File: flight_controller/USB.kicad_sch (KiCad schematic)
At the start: 11 parts, among them J9 TYPE-C16PIN2MD(073) (USB TYPE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, U5 SN74LVC1G07DBVR_C19829659

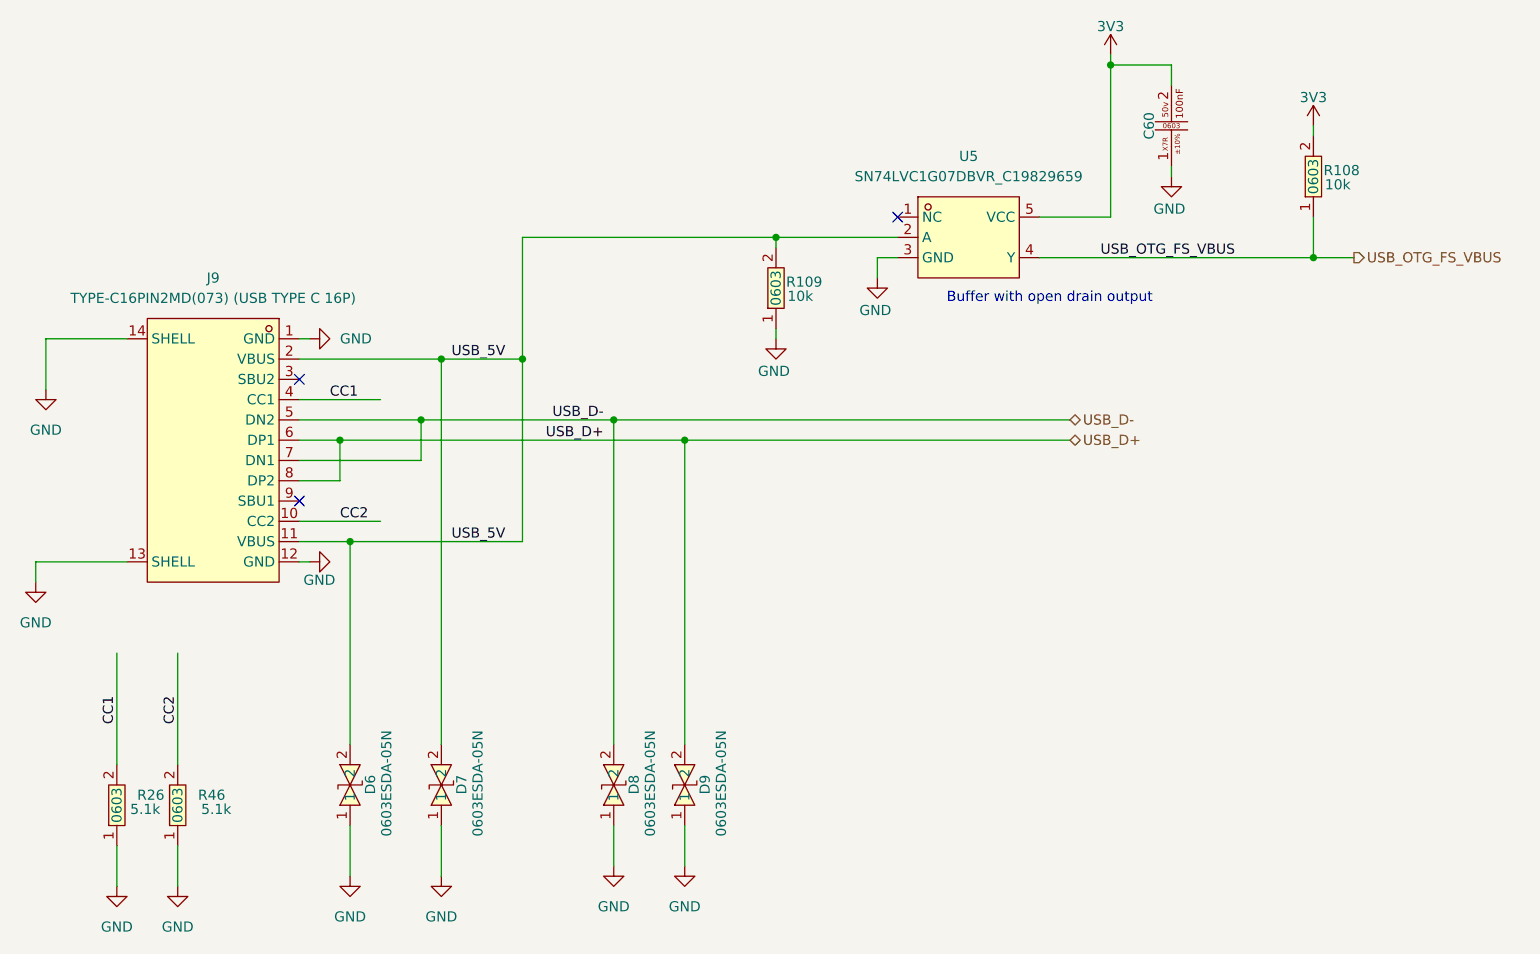
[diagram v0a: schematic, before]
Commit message: Started the placement process
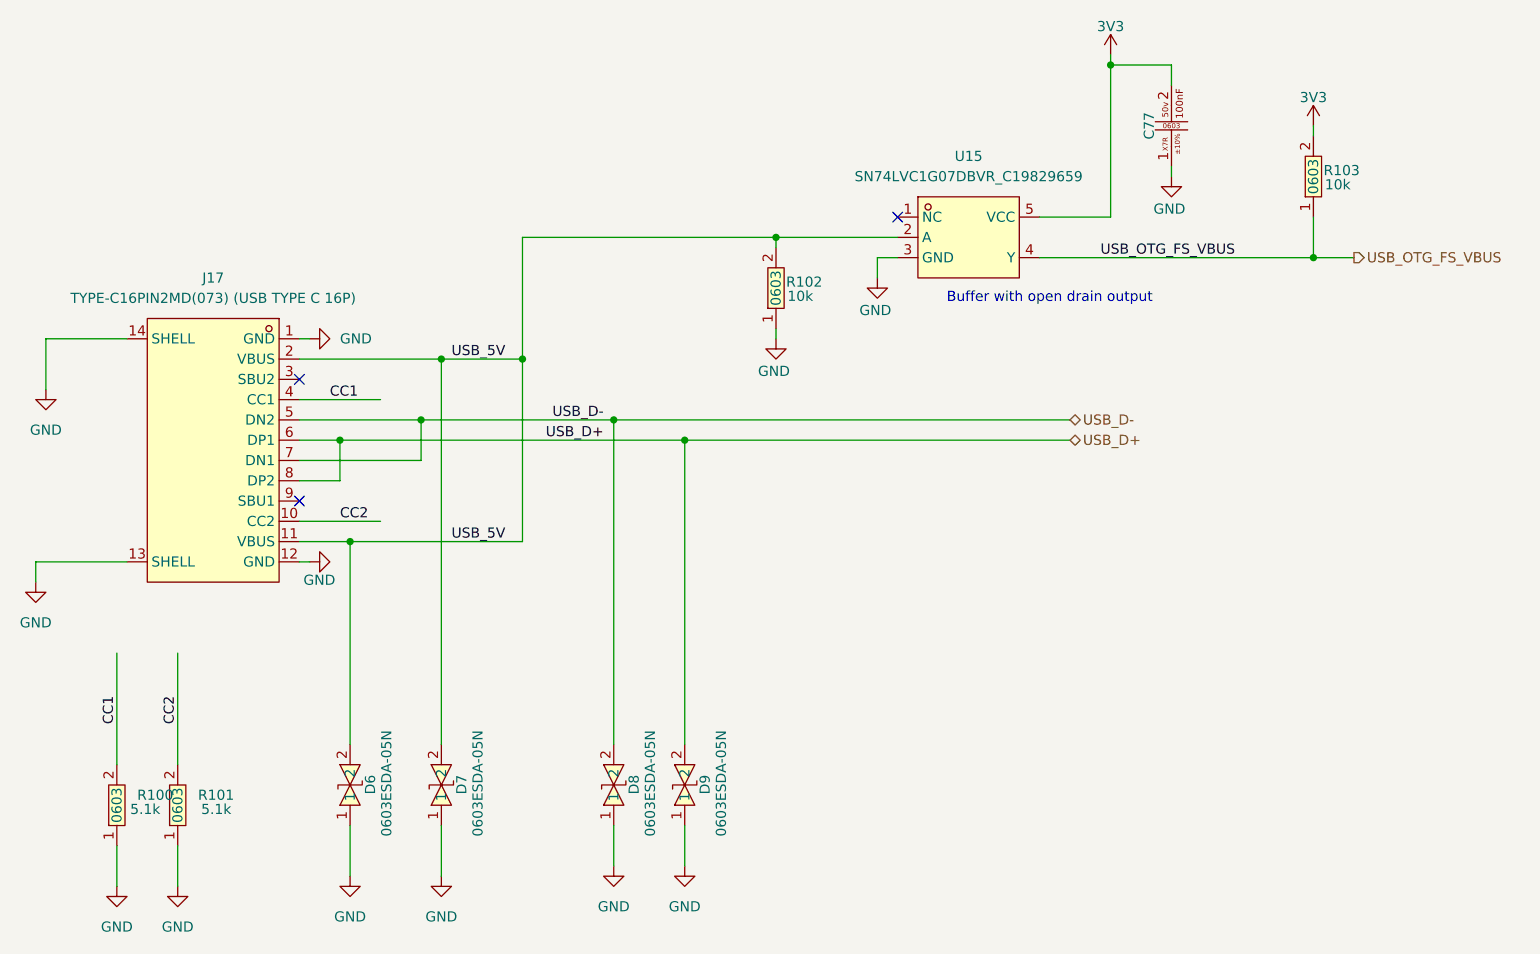
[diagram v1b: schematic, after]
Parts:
- renumbered C60 to C77, J9 to J17, R26 to R100, R46 to R101, R109 to R102, R108 to R103, U5 to U15
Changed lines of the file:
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@@
 		(on_board yes)
 		(dnp no)
-		(property "Reference" "#PWR0183"
+		(property "Reference" "#PWR0213"
 			(at 218.44 25.4 0)
 			(effects
@@
 			(project "FP_BOARD"
 				(path "/17737359-1a8e-4237-8899-d9604030bc1d/9d897fa1-9f20-45cb-8d2c-42b78b3f3ef1"
-					(reference "#PWR0183")
+					(reference "#PWR0213")
 					(unit 1)
 				)
@@
 		(dnp no)
 		(fields_autoplaced yes)
-		(property "Reference" "#PWR0415"
+		(property "Reference" "#PWR0208"
 			(at 134.62 130.81 0)
 			(effects
@@
 			(project "FP_BOARD"
 				(path "/17737359-1a8e-4237-8899-d9604030bc1d/9d897fa1-9f20-45cb-8d2c-42b78b3f3ef1"
-					(reference "#PWR0415")
+					(reference "#PWR0208")
 					(unit 1)
 				)
@@
 		(on_board yes)
 		(dnp no)
-		(property "Reference" "#PWR0412"
+		(property "Reference" "#PWR0206"
 			(at 124.46 85.09 0)
 			(effects
@@
 			(project "FP_BOARD"
 				(path "/17737359-1a8e-4237-8899-d9604030bc1d/9d897fa1-9f20-45cb-8d2c-42b78b3f3ef1"
-					(reference "#PWR0412")
+					(reference "#PWR0206")
 					(unit 1)
 				)
@@
 		(on_board yes)
 		(dnp no)
-		(property "Reference" "#PWR0195"
+		(property "Reference" "#PWR0211"
 			(at 176.53 63.5 0)
 			(effects
@@
 			(project "FP_BOARD"
 				(path "/17737359-1a8e-4237-8899-d9604030bc1d/9d897fa1-9f20-45cb-8d2c-42b78b3f3ef1"
-					(reference "#PWR0195")
+					(reference "#PWR0211")
 					(unit 1)
 				)
@@
 		(dnp no)
 		(fields_autoplaced yes)
-		(property "Reference" "#PWR0417"
+		(property "Reference" "#PWR0210"
 			(at 165.1 129.54 0)
 			(effects
@@
 			(project "FP_BOARD"
 				(path "/17737359-1a8e-4237-8899-d9604030bc1d/9d897fa1-9f20-45cb-8d2c-42b78b3f3ef1"
-					(reference "#PWR0417")
+					(reference "#PWR0210")
 					(unit 1)
 				)
@@
 		(on_board yes)
 		(dnp no)
-		(property "Reference" "#PWR0185"
+		(property "Reference" "#PWR0212"
 			(at 189.23 55.88 0)
 			(effects
@@
 			(project "FP_BOARD"
 				(path "/17737359-1a8e-4237-8899-d9604030bc1d/9d897fa1-9f20-45cb-8d2c-42b78b3f3ef1"
-					(reference "#PWR0185")
+					(reference "#PWR0212")
 					(unit 1)
 				)
@@
 		(dnp no)
 		(fields_autoplaced yes)
-		(property "Reference" "C60"
+		(property "Reference" "C77"
 			(at 223.266 30.48 0)
 			(do_not_autoplace yes)
@@
 			(project "FP_BOARD"
 				(path "/17737359-1a8e-4237-8899-d9604030bc1d/9d897fa1-9f20-45cb-8d2c-42b78b3f3ef1"
-					(reference "C60")
+					(reference "C77")
 					(unit 1)
 				)
@@
 		(on_board yes)
 		(dnp no)
-		(property "Reference" "#PWR0184"
+		(property "Reference" "#PWR0214"
 			(at 226.06 43.18 0)
 			(effects
@@
 			(project "FP_BOARD"
 				(path "/17737359-1a8e-4237-8899-d9604030bc1d/9d897fa1-9f20-45cb-8d2c-42b78b3f3ef1"
-					(reference "#PWR0184")
+					(reference "#PWR0214")
 					(unit 1)
 				)
@@
 		(dnp no)
 		(fields_autoplaced yes)
-		(property "Reference" "U5"
+		(property "Reference" "U15"
 			(at 200.66 34.29 0)
 			(effects
@@
 			(project ""
 				(path "/17737359-1a8e-4237-8899-d9604030bc1d/9d897fa1-9f20-45cb-8d2c-42b78b3f3ef1"
-					(reference "U5")
+					(reference "U15")
 					(unit 1)
 				)
@@
 		(on_board yes)
 		(dnp no)
-		(property "Reference" "R46"
+		(property "Reference" "R101"
 			(at 104.14 114.2999 90)
 			(effects
@@
 			(project "FP_BOARD"
 				(path "/17737359-1a8e-4237-8899-d9604030bc1d/9d897fa1-9f20-45cb-8d2c-42b78b3f3ef1"
-					(reference "R46")
+					(reference "R101")
 					(unit 1)
 				)
@@
 		(dnp no)
 		(fields_autoplaced yes)
-		(property "Reference" "J9"
+		(property "Reference" "J17"
 			(at 106.045 49.53 0)
 			(effects
@@
 			(project ""
 				(path "/17737359-1a8e-4237-8899-d9604030bc1d/9d897fa1-9f20-45cb-8d2c-42b78b3f3ef1"
-					(reference "J9")
+					(reference "J17")
 					(unit 1)
 				)
@@
 		(dnp no)
 		(fields_autoplaced yes)
-		(property "Reference" "#PWR0411"
+		(property "Reference" "#PWR0201"
 			(at 83.82 93.98 0)
 			(effects
@@
 			(project "FP_BOARD"
 				(path "/17737359-1a8e-4237-8899-d9604030bc1d/9d897fa1-9f20-45cb-8d2c-42b78b3f3ef1"
-					(reference "#PWR0411")
+					(reference "#PWR0201")
 					(unit 1)
 				)
@@
 		(on_board yes)
 		(dnp no)
-		(property "Reference" "R109"
+		(property "Reference" "R102"
 			(at 177.8 50.038 90)
 			(effects
@@
 			(project "FP_BOARD"
 				(path "/17737359-1a8e-4237-8899-d9604030bc1d/9d897fa1-9f20-45cb-8d2c-42b78b3f3ef1"
-					(reference "R109")
+					(reference "R102")
 					(unit 1)
 				)
@@
 		(on_board yes)
 		(dnp no)
-		(property "Reference" "R108"
+		(property "Reference" "R103"
 			(at 245.11 36.068 90)
 			(effects
@@
 			(project "FP_BOARD"
 				(path "/17737359-1a8e-4237-8899-d9604030bc1d/9d897fa1-9f20-45cb-8d2c-42b78b3f3ef1"
-					(reference "R108")
+					(reference "R103")
 					(unit 1)
 				)
@@
 		(on_board yes)
 		(dnp no)
-		(property "Reference" "#PWR0186"
+		(property "Reference" "#PWR0215"
 			(at 243.84 34.29 0)
 			(effects
@@
 			(project "FP_BOARD"
 				(path "/17737359-1a8e-4237-8899-d9604030bc1d/9d897fa1-9f20-45cb-8d2c-42b78b3f3ef1"
-					(reference "#PWR0186")
+					(reference "#PWR0215")
 					(unit 1)
 				)
@@
 		(dnp no)
 		(fields_autoplaced yes)
-		(property "Reference" "#PWR0418"
+		(property "Reference" "#PWR0203"
 			(at 93.98 132.08 0)
 			(effects
@@
 			(project "FP_BOARD"
 				(path "/17737359-1a8e-4237-8899-d9604030bc1d/9d897fa1-9f20-45cb-8d2c-42b78b3f3ef1"
-					(reference "#PWR0418")
+					(reference "#PWR0203")
 					(unit 1)
 				)
@@
 		(dnp no)
 		(fields_autoplaced yes)
-		(property "Reference" "#PWR0414"
+		(property "Reference" "#PWR0207"
 			(at 123.19 130.81 0)
 			(effects
@@
 			(project "FP_BOARD"
 				(path "/17737359-1a8e-4237-8899-d9604030bc1d/9d897fa1-9f20-45cb-8d2c-42b78b3f3ef1"
-					(reference "#PWR0414")
+					(reference "#PWR0207")
 					(unit 1)
 				)
@@
 		(dnp no)
 		(fields_autoplaced yes)
-		(property "Reference" "#PWR0413"
+		(property "Reference" "#PWR0205"
 			(at 124.46 57.15 0)
 			(effects
@@
 			(project "FP_BOARD"
 				(path "/17737359-1a8e-4237-8899-d9604030bc1d/9d897fa1-9f20-45cb-8d2c-42b78b3f3ef1"
-					(reference "#PWR0413")
+					(reference "#PWR0205")
 					(unit 1)
 				)
@@
 		(dnp no)
 		(fields_autoplaced yes)
-		(property "Reference" "#PWR0416"
+		(property "Reference" "#PWR0209"
 			(at 156.21 129.54 0)
 			(effects
@@
 			(project "FP_BOARD"
 				(path "/17737359-1a8e-4237-8899-d9604030bc1d/9d897fa1-9f20-45cb-8d2c-42b78b3f3ef1"
-					(reference "#PWR0416")
+					(reference "#PWR0209")
 					(unit 1)
 				)
@@
 		(dnp no)
 		(fields_autoplaced yes)
-		(property "Reference" "#PWR0419"
+		(property "Reference" "#PWR0204"
 			(at 101.6 132.08 0)
 			(effects
@@
 			(project "FP_BOARD"
 				(path "/17737359-1a8e-4237-8899-d9604030bc1d/9d897fa1-9f20-45cb-8d2c-42b78b3f3ef1"
-					(reference "#PWR0419")
+					(reference "#PWR0204")
 					(unit 1)
 				)
@@
 		(dnp no)
 		(fields_autoplaced yes)
-		(property "Reference" "#PWR0410"
+		(property "Reference" "#PWR0202"
 			(at 85.09 69.85 0)
 			(effects
@@
 			(project "FP_BOARD"
 				(path "/17737359-1a8e-4237-8899-d9604030bc1d/9d897fa1-9f20-45cb-8d2c-42b78b3f3ef1"
-					(reference "#PWR0410")
+					(reference "#PWR0202")
 					(unit 1)
 				)
@@
 		(on_board yes)
 		(dnp no)
-		(property "Reference" "R26"
+		(property "Reference" "R100"
 			(at 96.52 114.2999 90)
 			(effects
@@
 			(project "FP_BOARD"
 				(path "/17737359-1a8e-4237-8899-d9604030bc1d/9d897fa1-9f20-45cb-8d2c-42b78b3f3ef1"
-					(reference "R26")
-					(unit 1)
-				)
+					(reference "R100")
+					(unit 1)
+				)

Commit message: renamed some connectors to j instead of cn
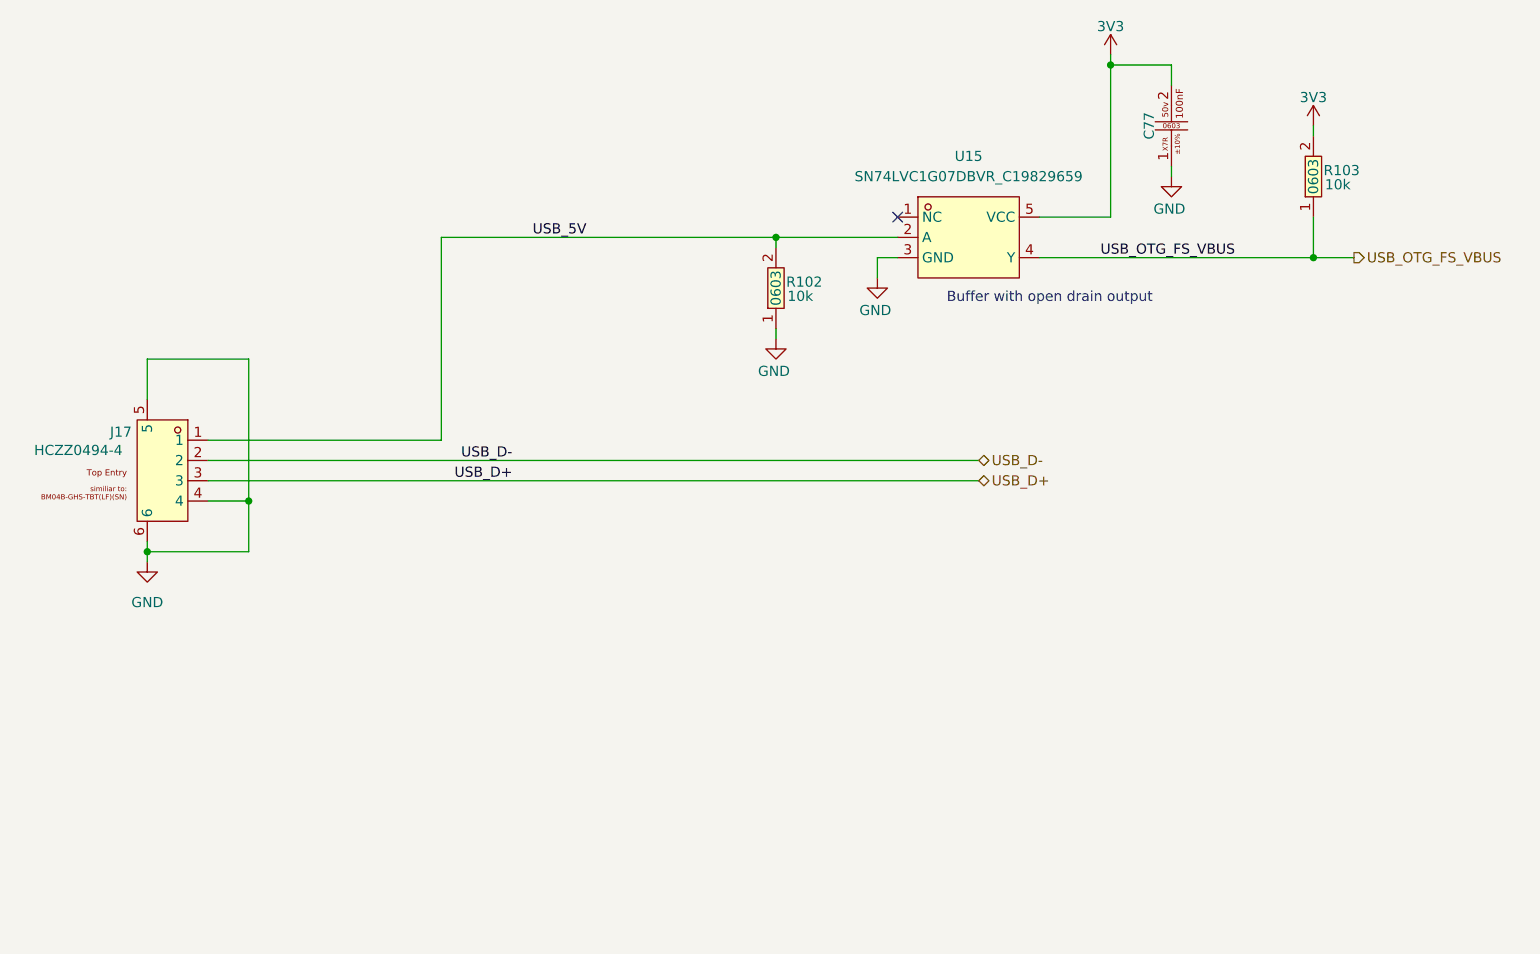
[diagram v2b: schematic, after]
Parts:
- removed D6, D7, D8, D9: 0603ESDA-05N, easyeda2kicad:D0603-BI, symbol easyeda2kicad:0603ESDA-05N
- removed J17: TYPE-C16PIN2MD(073) (USB TYPE C 16P), easyeda2kicad:USB-C-SMD_TYPE-C-6PIN-2MD-073, symbol lampelKicadLIB:TYPE-C16PIN2MD(073) (USB TYPE C 16P)
- removed R100, R101: 0603WAF5101T5E, easyeda2kicad:R0603, symbol easyeda2kicad:0603WAF5101T5E
- added J17: HCZZ0494-4, easyeda2kicad:CONN-SMD_4P-P1.25_BM04B-GHS-TBT-LF-SN, symbol easyeda_lampel:HCZZ0494-4
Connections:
- net GND: now also J17.4, J17.5, J17.6
- net USB_5V: now also J17.1
- net USB_D+: now also J17.3
- net USB_D-: now also J17.2
- no-connect marks 3 -> 1

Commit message: Advanced in routing
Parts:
- added C82: CC0603KRX7R9BB104 (100nf , 0603 ,50v ,X7R), easyeda2kicad:C0603, symbol lampelKicadLIB:CC0603KRX7R9BB104 (100nf , 0603 ,50v ,X7R)
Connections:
- net GND: now also C82.1
- net USB_5V: now also C82.2
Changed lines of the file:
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@@
+		(color 0 0 0 0)
+	)
+	(junction
+		(at 134.62 48.26)
+		(diameter 0)
 		(color 0 0 0 0)
 	)
@@
 	(wire
 		(pts
+			(xy 144.78 63.5) (xy 144.78 62.23)
+		)
+		(stroke
+			(width 0)
+			(type default)
+		)
+	)
+	(wire
+		(pts
 			(xy 110.49 59.69) (xy 110.49 77.47)
 		)
@@
 	(wire
 		(pts
+			(xy 144.78 52.07) (xy 144.78 48.26)
+		)
+		(stroke
+			(width 0)
+			(type default)
+		)
+	)
+	(wire
+		(pts
 			(xy 189.23 46.99) (xy 189.23 49.53)
 		)
@@
 	(wire
 		(pts
+			(xy 144.78 48.26) (xy 134.62 48.26)
+		)
+		(stroke
+			(width 0)
+			(type default)
+		)
+	)
+	(wire
+		(pts
 			(xy 110.49 83.82) (xy 97.79 83.82)
 		)
@@
 	(wire
 		(pts
-			(xy 134.62 44.45) (xy 134.62 69.85)
+			(xy 134.62 44.45) (xy 134.62 48.26)
+		)
+		(stroke
+			(width 0)
+			(type default)
+		)
+	)
+	(wire
+		(pts
+			(xy 134.62 48.26) (xy 134.62 69.85)
 		)
 		(stroke
@@
 	)
 	(symbol
+		(lib_id "lampelKicadLIB:CC0603KRX7R9BB104 (100nf , 0603 ,50v ,X7R)")
+		(at 144.78 57.15 90)
+		(unit 1)
+		(exclude_from_sim no)
+		(in_bom yes)
+		(on_board yes)
+		(dnp no)
+		(fields_autoplaced yes)
+		(property "Reference" "C82"
+			(at 141.986 57.15 0)
+			(do_not_autoplace yes)
+			(effects
+				(font
+					(size 1.27 1.27)
+				)
+			)
+		)
+		(property "Value" "CC0603KRX7R9BB104 (100nf , 0603 ,50v ,X7R)"
+			(at 149.86 57.15 0)
+			(effects
+				(font
+					(size 1.27 1.27)
+				)
+				(hide yes)
+			)
+		)
+		(property "Footprint" "easyeda2kicad:C0603"
+			(at 152.4 57.15 0)
+			(effects
+				(font
+					(size 1.27 1.27)
+				)
+				(hide yes)
+			)
+		)
+		(property "Datasheet" "https://lcsc.com/product-detail/Multilayer-Ceramic-Capacitors-MLCC-SMD-SMT_100nF-104-10-50V_C14663.html"
+			(at 154.94 57.15 0)
+			(effects
+				(font
+					(size 1.27 1.27)
+				)
+				(hide yes)
+			)
+		)
+		(property "Description" "100nF ±10% 50V Ceramic Capacitor X7R 0603"
+			(at 144.78 57.15 0)
+			(effects
+				(font
+					(size 1.27 1.27)
+				)
+				(hide yes)
+			)
+		)
+		(property "LCSC Part" "C14663"
+			(at 157.48 57.15 0)
+			(effects
+				(font
+					(size 1.27 1.27)
+				)
+				(hide yes)
+			)
+		)
+		(pin "1"
+		)
+		(pin "2"
+		)
+		(instances
+			(project "FP_BOARD"
+				(path "/17737359-1a8e-4237-8899-d9604030bc1d/9d897fa1-9f20-45cb-8d2c-42b78b3f3ef1"
+					(reference "C82")
+					(unit 1)
+				)
+			)
+		)
+	)
+	(symbol
 		(lib_id "power:GND")
 		(at 226.06 36.83 0)
@@
 					(unit 1)
 				)
+			)
+		)
+	)
+	(symbol
+		(lib_id "power:GND")
+		(at 144.78 63.5 0)
+		(unit 1)
+		(exclude_from_sim no)
+		(in_bom yes)
+		(on_board yes)
+		(dnp no)
+		(fields_autoplaced yes)
+		(property "Reference" "#PWR0204"
+			(at 144.78 69.85 0)
+			(effects
+				(font
+					(size 1.27 1.27)
+				)
+				(hide yes)
+			)
+		)
+		(property "Value" "GND"
+			(at 144.78 68.58 0)
+			(effects
+				(font
+					(size 1.27 1.27)
+				)
+			)
+		)
+		(property "Footprint" ""
+			(at 144.78 63.5 0)
+			(effects
+				(font
+					(size 1.27 1.27)
+				)
+				(hide yes)
+			)
+		)
+		(property "Datasheet" ""
+			(at 144.78 63.5 0)
+			(effects
+				(font
+					(size 1.27 1.27)
+				)
+				(hide yes)
+			)
+		)
+		(property "Description" ""
+			(at 144.78 63.5 0)
+			(effects
+				(font
+					(size 1.27 1.27)
+				)
+				(hide yes)
+			)
+		)
+		(pin "1"
+		)
+		(instances
+			(project "FP_BOARD"
+				(path "/17737359-1a8e-4237-8899-d9604030bc1d/9d897fa1-9f20-45cb-8d2c-42b78b3f3ef1"
+					(reference "#PWR0204")
+					(unit 1)
+				)
